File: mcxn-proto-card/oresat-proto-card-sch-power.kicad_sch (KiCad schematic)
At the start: 90 parts, among them Q1 DMP2240UDM, Q2 DMP3050LVT-7, Q7 MOSFET-PCH-SOT23-6, Q8 PMV45EN, Q9 PMV45EN, U10 TPS62111RSA, U11 MIC842LYC5, U12 MIC842LYC5, U2 MAX7310, U3 TS5A21366DCUR, U6 MAX4211

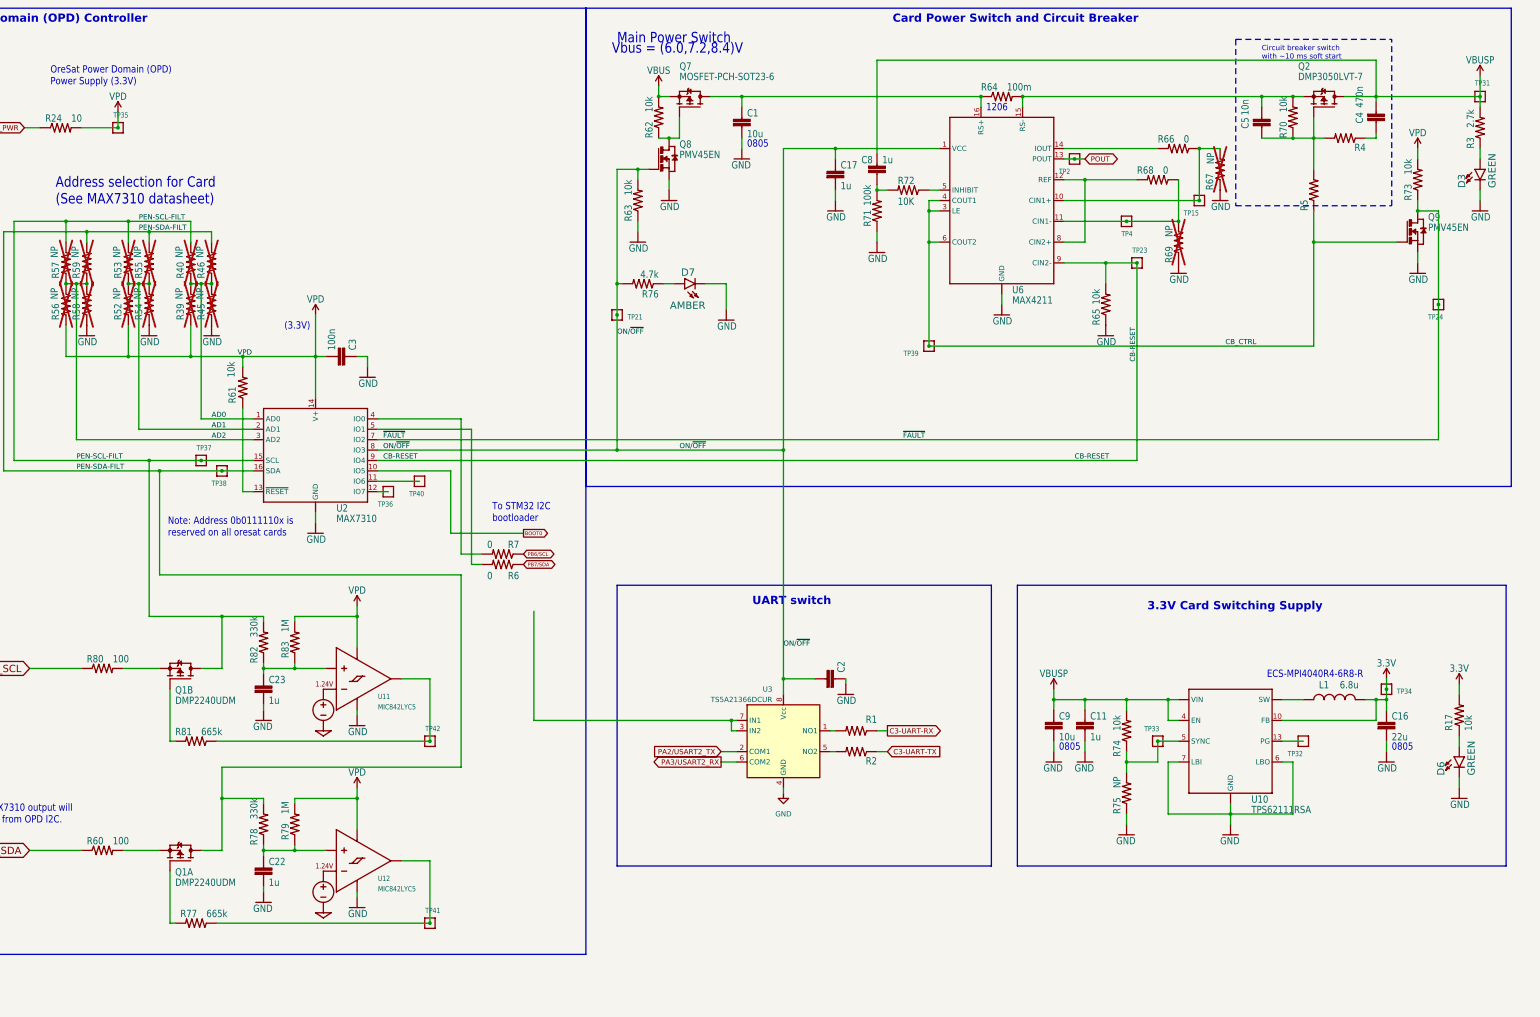
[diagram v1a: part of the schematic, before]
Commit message: Removed and replaced eagle libraries for C, R, and Power symbols
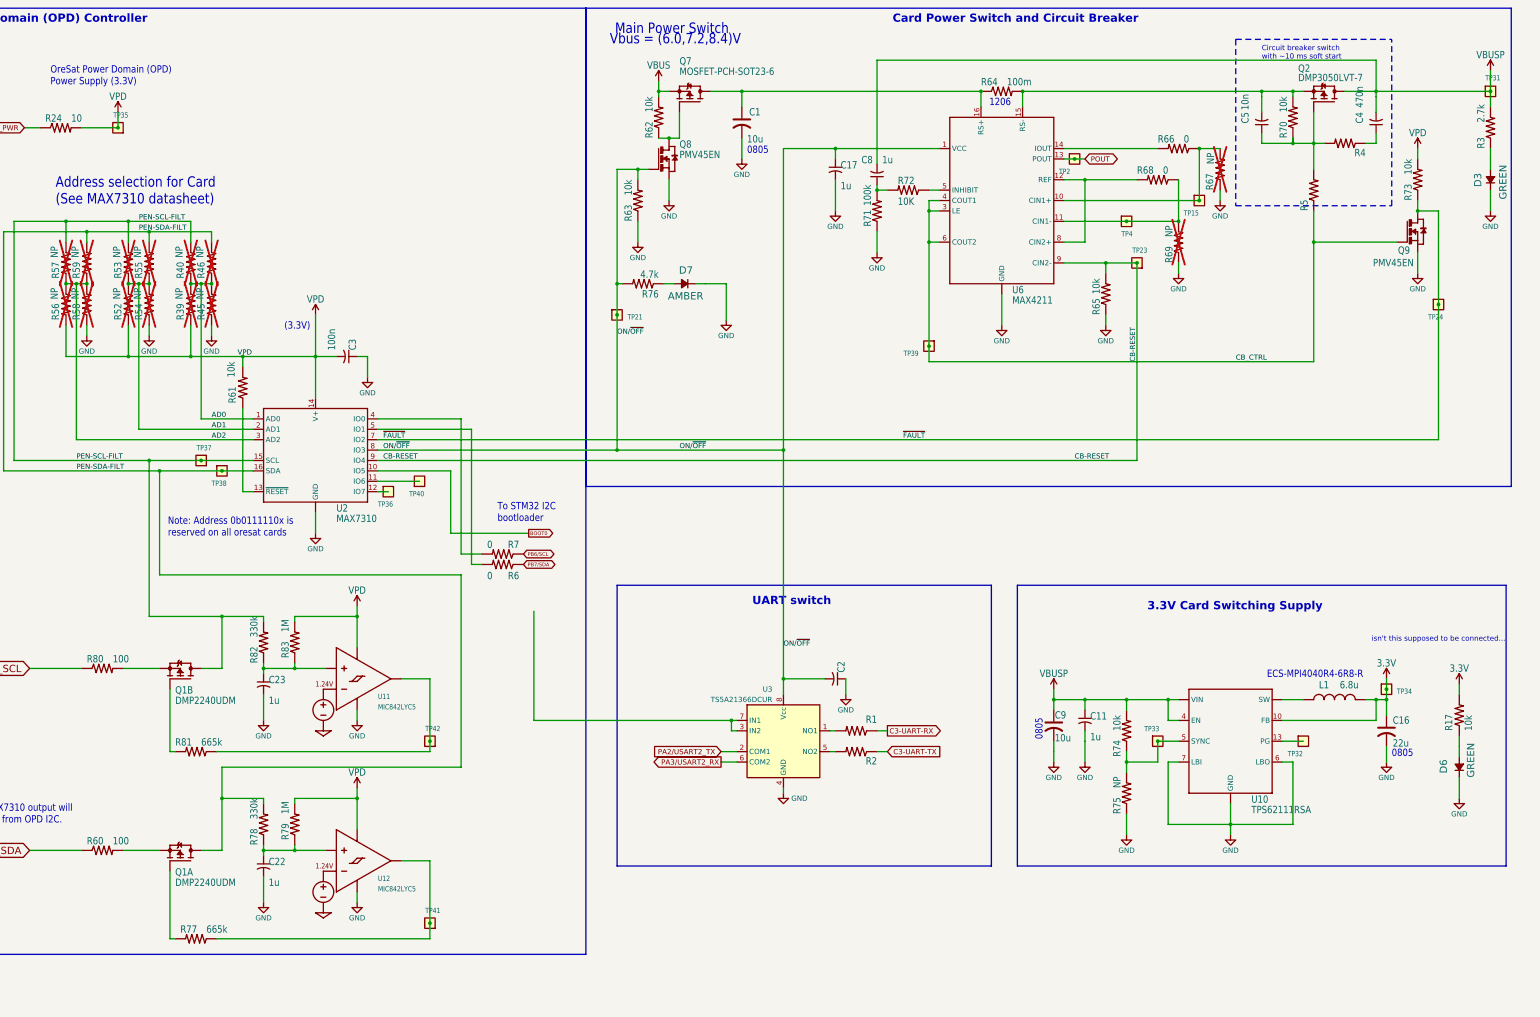
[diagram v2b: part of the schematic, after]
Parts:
- C1, C16, C9: symbol oresat-proto-card-eagle-import:C-EU0805-B-NOSILK -> Device:C_US
- C11, C17, C2, C22, C23, C3, C4, C5, C8: symbol oresat-proto-card-eagle-import:C-EU0603-C-NOSILK -> Device:C_Small_US
- D3, D6, D7: symbol oresat-proto-card-eagle-import:LED-GREEN0603 -> Device:D_Small_Filled
- R1, R17, R2, R24, R3, R39, R4, R40, R45, R46, R5, R52, R53, R54, R55, R56, R57, R58, R59, R6, R60, R61, R62, R63, R65, R66, R67, R68, R69, R7, R70, R71, R72, R73, R74, R75, R76, R77, R78, R79, R80, R81, R82, R83: symbol oresat-proto-card-eagle-import:R-US_0603-C-NOSILK -> oresat-passives:R-US
- TP15, TP2, TP21, TP23, TP24, TP31, TP32, TP33, TP34, TP35, TP36, TP37, TP38, TP39, TP4, TP40, TP41, TP42: value TEST-POINT-LARGE-SQUARE -> Test-Point; footprint oresat-proto-card:1X01 -> oresat-misc:TestPoint-0.75mm-th; symbol oresat-proto-card-eagle-import:TEST-POINT-LARGE-SQUARE -> oresat-misc:Test-Point-0.75mm-th; now left out of the parts list
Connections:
- net CB_CTRL is gone; now on net CB-RESET: Q9.1 (G), R5.1, TP39.1, U6.3 (LE), U6.4 (COUT1), U6.6 (COUT2)
- net GND: now also D3.1 (K), D6.1 (K), D7.1 (K); no longer D3.C, D6.C, D7.C
- net at R3.1: now also D3.2 (A); no longer D3.A
- net at R76.1: now also D7.2 (A); no longer D7.A
- net at R17.1: now also D6.2 (A); no longer D6.A
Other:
- note added: "isn't this supposed to be connected..."
- moved on the sheet: Q2, Q7, R3, R4, R64, R65, R77, R81

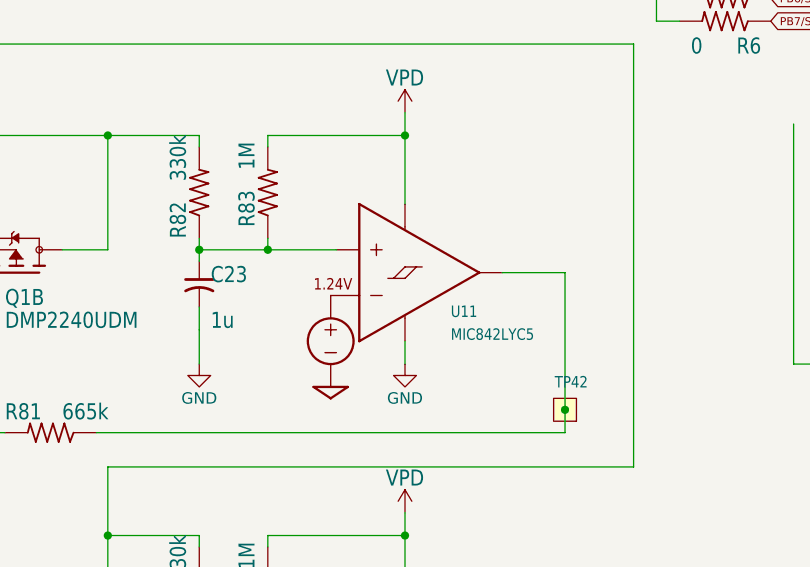
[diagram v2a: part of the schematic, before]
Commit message: Removed and replaced Eagle libraries for MOSFET
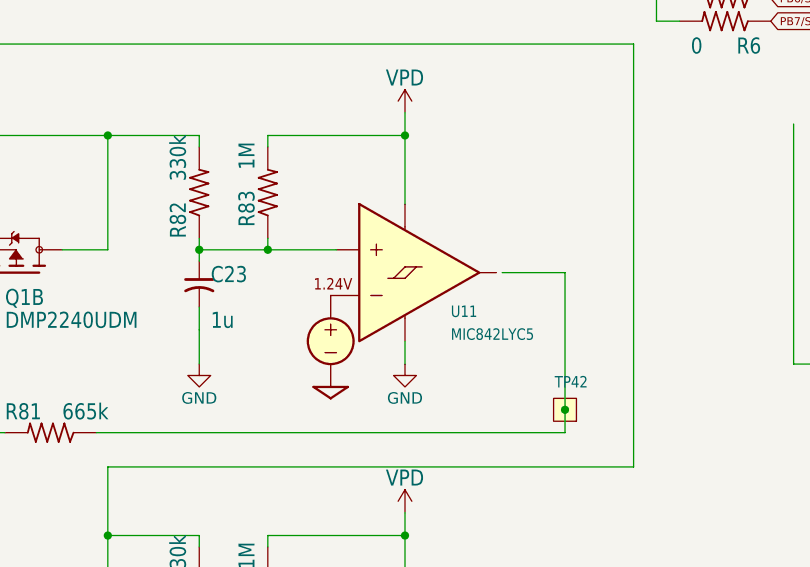
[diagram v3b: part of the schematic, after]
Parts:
- U11: footprint oresat-proto-card:SC70-5 -> Package_TO_SOT_SMD:SOT-353_SC-70-5; symbol oresat-proto-card-eagle-import:MIC842LYC5 -> oresat-ics:MIC842LYC5
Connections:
- net at R81.1, TP42.1: no longer U11.4 (OUT)
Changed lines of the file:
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@@
 	)
 	(symbol
-		(lib_id "oresat-proto-card-eagle-import:MIC842LYC5")
+		(lib_id "oresat-ics:MIC842LYC5")
 		(at 129.54 179.07 0)
 		(unit 1)
@@
 			)
 		)
-		(property "Footprint" "oresat-proto-card:SC70-5"
-			(at 129.54 179.07 0)
+		(property "Footprint" "Package_TO_SOT_SMD:SOT-353_SC-70-5"
+			(at 129.794 157.226 0)
 			(effects
 				(font
@@
 			)
 		)
-		(property "Datasheet" ""
-			(at 129.54 179.07 0)
+		(property "Datasheet" "https://ww1.microchip.com/downloads/aemDocuments/documents/OTH/ProductDocuments/DataSheets/20005758A.pdf"
+			(at 129.54 159.512 0)
 			(effects
 				(font
@@
 			)
 		)
-		(property "Description" ""
-			(at 129.54 179.07 0)
+		(property "Description" "IC Single Comparator W/REF, SC-70-5"
+			(at 129.54 161.798 0)
 			(effects
 				(font
 					(size 1.27 1.27)
 				)
+				(hide yes)
 			)
 		)
@@
 		(pin "4"
 		)
+		(pin "3"
+		)
 		(instances

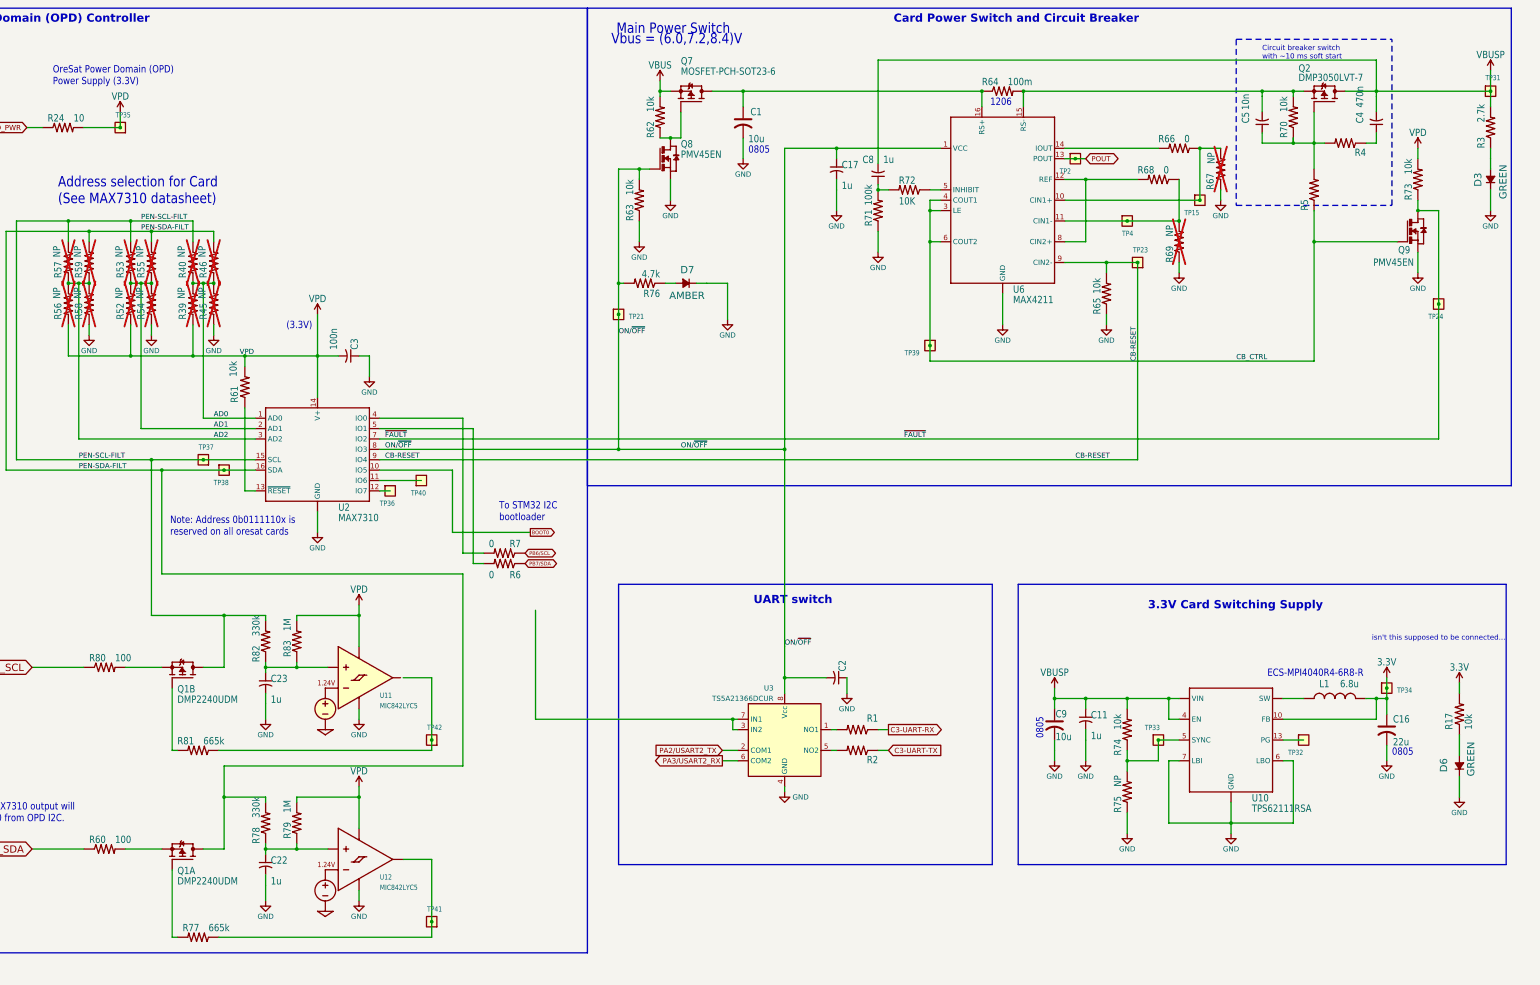
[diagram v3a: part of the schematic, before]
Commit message: Eagle libraries removed and replaced, schematic and layout clean up
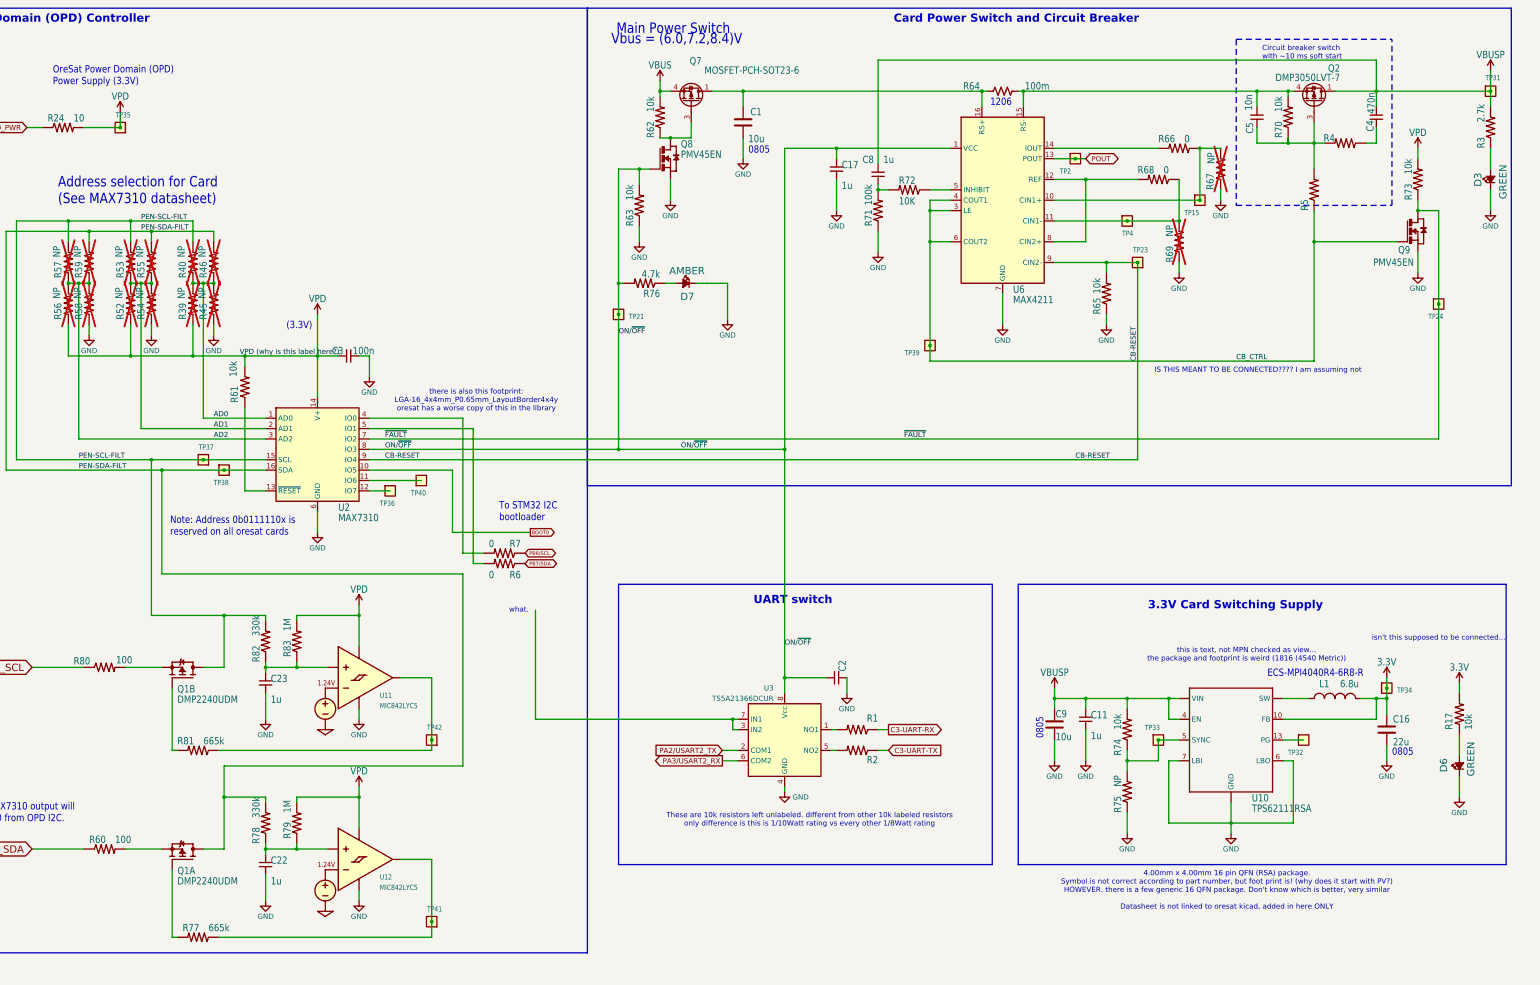
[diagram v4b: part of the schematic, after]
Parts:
- C1, C16, C9: symbol Device:C_US -> Device:C
- C11, C17, C2, C22, C23, C3, C4, C5, C8: symbol Device:C_Small_US -> Device:C_Small
- D3, D6, D7: footprint oresat-proto-card:LED-0603 -> LED_SMD:LED_0603_1608Metric; symbol Device:D_Small_Filled -> Device:LED_Small_Filled
- L1: symbol oresat-proto-card-eagle-import:L-ECS-MPI4040 -> oresat-passives:L_BIG
- Q1: footprint oresat-proto-card:SOT23-6 -> Package_TO_SOT_SMD:SOT-23-6; symbol oresat-proto-card-eagle-import:Q-MOSFET-PCH-dual-SOT23-6_MOSFET-PCH-SOT23-6 -> oresat-transistors:DMP2240UDM-7
- Q2, Q7: footprint oresat-proto-card:SOT23-6 -> Package_TO_SOT_SMD:SOT-23-6; symbol oresat-proto-card-eagle-import:MOSFET-PCH-SOT23-6 -> oresat-transistors:DMP3050LVT-7
- R64: footprint oresat-proto-card:R1206 -> oresat-passives:1206-C; symbol oresat-proto-card-eagle-import:rcl_R-US_R1206 -> Device:R_US
- U12: footprint oresat-proto-card:SC70-5 -> Package_TO_SOT_SMD:SOT-353_SC-70-5; symbol oresat-proto-card-eagle-import:MIC842LYC5 -> oresat-ics:MIC842LYC5
- U2: footprint oresat-proto-card:QFN65P400X400X80-17T210 -> Package_DFN_QFN:QFN-16-1EP_4x4mm_P0.65mm_EP2.1x2.1mm; symbol oresat-proto-card-eagle-import:MAX7310 -> oresat-ics:MAX7310
- U6: footprint oresat-proto-card:QFN65P400X400X80-17T210 -> Package_DFN_QFN:QFN-16-1EP_4x4mm_P0.65mm_EP2.1x2.1mm; symbol oresat-proto-card-eagle-import:MAX4211 -> oresat-ics:MAX4211FETE
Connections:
- net GND: now also U2.17 (GND), U6.17 (GND); no longer U2.EPAD (GND), U6.EPAD (GND)
- net at U11.4 (OUT): now also R81.1, TP42.1
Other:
- note added: "4.00mm x 4.00mm 16 pin QFN (RSA) package. Symbol is not correct according to part number, but foot print is! (why does it start with PV?) HOWEVER. there is a few generic 16 QFN package. Don't know which is better, very similar Datasheet is not linked to oresat kicad, added in here ONLY"
- note added: "IS THIS MEANT TO BE CONNECTED???? I am assuming not"
- note added: "These are 10k resistors left unlabeled. different from other 10k labeled resistors only difference is this is 1/10Watt rating vs every other 1/8Watt rating"
- note added: "there is also this footprint: LGA-16_4x4mm_P0.65mm_LayoutBorder4x4y oresat has a worse copy of this in the library"
- note added: "this is text, not MPN checked as view... the package and footprint is weird (1816 (4540 Metric))"
- note added: "what."
- moved on the sheet: C4, C5, R63, R70
